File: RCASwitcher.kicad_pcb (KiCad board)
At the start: 2 copper layers, 128.5 x 75.5 mm, 13 parts, among them J1 Connector_RCA_2x3_REB, J2 Connector_RCA_2x3_REB, J3 Connector_RCA_2x3_REB, J4 Connector_RCA_2x3_REB, J5 Connector_RCA_2x3_REB, J6 Connector_RCA_2x3_REB, SW1 SW_SPDT_3x2_REB, SW2 SW_SPDT_3x2_REB, SW3 SW_SPDT_3x2_REB, SW4 SW_SPDT_3x2_REB, SW5 SW_SPDT_3x2_REB

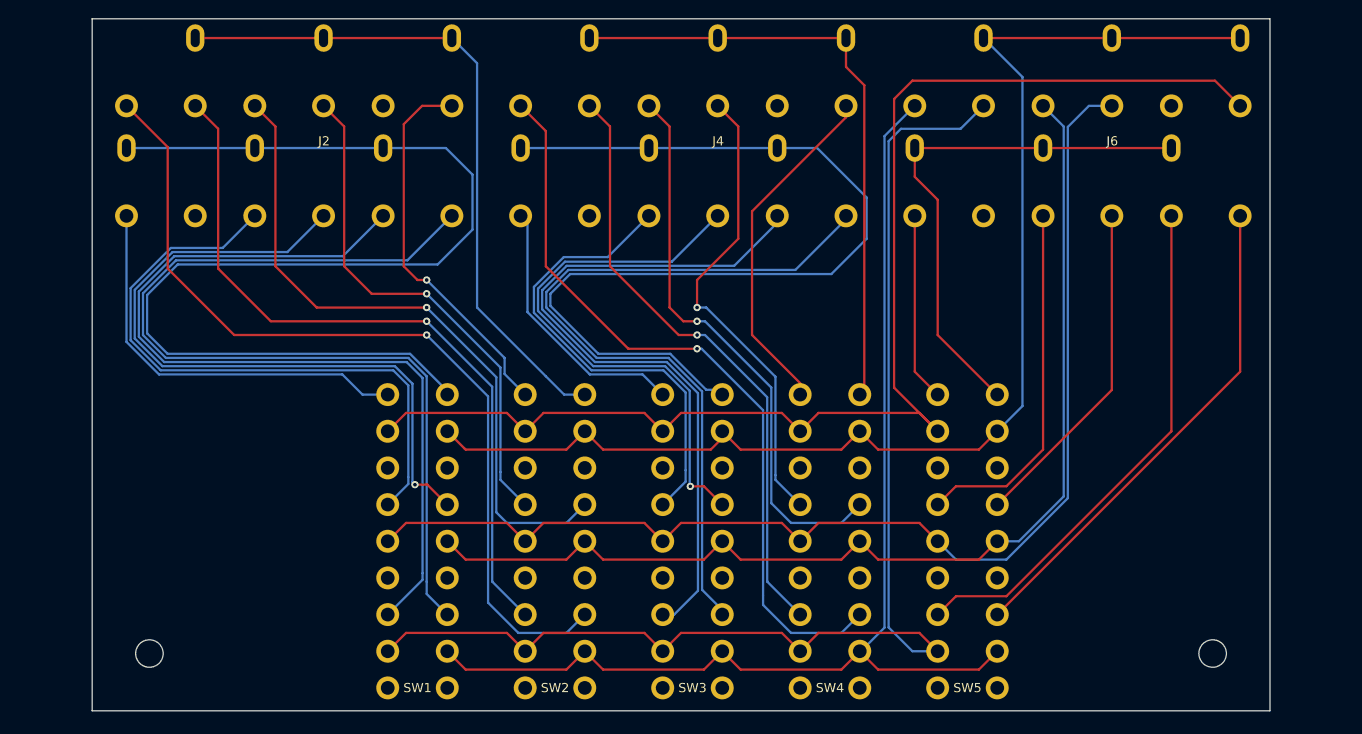
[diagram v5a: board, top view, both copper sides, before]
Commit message: Expand board a little to add mount points
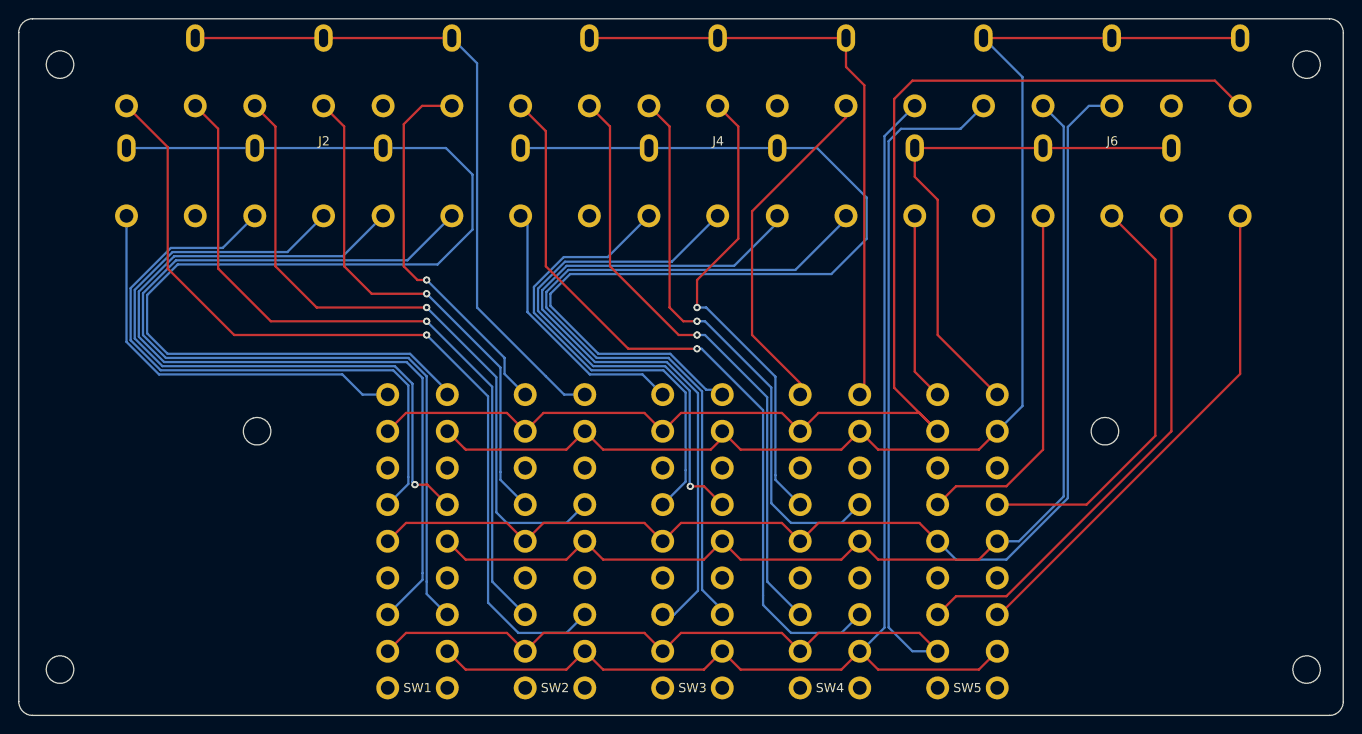
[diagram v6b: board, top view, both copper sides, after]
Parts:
- added REF**: MountingHole_3mm, MountingHole:MountingHole_3mm, F.Cu at (28.0, 70.0)
- added REF**: MountingHole_3mm, MountingHole:MountingHole_3mm, F.Cu at (142.0, 110.0)
- added REF**: MountingHole_3mm, MountingHole:MountingHole_3mm, F.Cu at (49.5, 110.0)
- added REF**: MountingHole_3mm, MountingHole:MountingHole_3mm, F.Cu at (164.0, 70.0)
- moved REF** 10.4 mm to (164.0, 136.0)
- moved REF** 9.91 mm to (28.0, 136.0)
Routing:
- net /R_5: track 36.7 -> 46.3 mm
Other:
- board size 128.5 x 75.5 mm -> 144.5 x 76 mm
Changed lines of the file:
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@@
       (net 28 "/GND_4") (pinfunction "GND") (pintype "passive"))
+  )
+  (footprint "MountingHole:MountingHole_3mm" (layer "F.Cu")
+    (at 28 70)
+    (descr "Mounting Hole 3mm, no annular")
+    (tags "mounting hole 3mm no annular")
+    (attr exclude_from_pos_files exclude_from_bom)
+    (fp_text reference "REF**" (at 0 -4) (layer "F.SilkS") hide
+      (effects (font (size 1 1) (thickness 0.15)))
+    )
+    (fp_text value "MountingHole_3mm" (at 0 4) (layer "F.Fab")
+      (effects (font (size 1 1) (thickness 0.15)))
+    )
+    (fp_text user "${REFERENCE}" (at 0 0) (layer "F.Fab")
+      (effects (font (size 1 1) (thickness 0.15)))
+    )
+    (fp_circle (center 0 0) (end 3 0) (layer "Cmts.User") (width 0.15) (fill none))
+    (fp_circle (center 0 0) (end 3.25 0) (layer "F.CrtYd") (width 0.05) (fill none))
+    (pad "" np_thru_hole circle (at 0 0) (size 3 3) (drill 3) (layers *.Cu *.Mask))
   )
   (footprint "User:SW_SPDT_3x2_REB" (layer "F.Cu")
@@
       (net 35 "/GND_5") (pinfunction "C") (pintype "passive"))
   )
+  (footprint "MountingHole:MountingHole_3mm" (layer "F.Cu")
+    (at 142 110)
+    (descr "Mounting Hole 3mm, no annular")
+    (tags "mounting hole 3mm no annular")
+    (attr exclude_from_pos_files exclude_from_bom)
+    (fp_text reference "REF**" (at 0 -4) (layer "F.SilkS") hide
+      (effects (font (size 1 1) (thickness 0.15)))
+    )
+    (fp_text value "MountingHole_3mm" (at 0 4) (layer "F.Fab")
+      (effects (font (size 1 1) (thickness 0.15)))
+    )
+    (fp_text user "${REFERENCE}" (at 0 0) (layer "F.Fab")
+      (effects (font (size 1 1) (thickness 0.15)))
+    )
+    (fp_circle (center 0 0) (end 3 0) (layer "Cmts.User") (width 0.15) (fill none))
+    (fp_circle (center 0 0) (end 3.25 0) (layer "F.CrtYd") (width 0.05) (fill none))
+    (pad "" np_thru_hole circle (at 0 0) (size 3 3) (drill 3) (layers *.Cu *.Mask))
+  )
   (footprint "User:Connector_RCA_2x3_REB" (layer "F.Cu")
     (at 142.75 74.5)
@@
     (pad "9" thru_hole oval (at -14 -7.4) (size 2 3) (drill oval 1 2) (layers *.Cu *.Mask)
       (net 42 "/GND_out") (pinfunction "GND") (pintype "passive"))
+  )
+  (footprint "MountingHole:MountingHole_3mm" (layer "F.Cu")
+    (at 49.5 110)
+    (descr "Mounting Hole 3mm, no annular")
+    (tags "mounting hole 3mm no annular")
+    (attr exclude_from_pos_files exclude_from_bom)
+    (fp_text reference "REF**" (at 0 -4) (layer "F.SilkS") hide
+      (effects (font (size 1 1) (thickness 0.15)))
+    )
+    (fp_text value "MountingHole_3mm" (at 0 4) (layer "F.Fab")
+      (effects (font (size 1 1) (thickness 0.15)))
+    )
+    (fp_text user "${REFERENCE}" (at 0 0) (layer "F.Fab")
+      (effects (font (size 1 1) (thickness 0.15)))
+    )
+    (fp_circle (center 0 0) (end 3 0) (layer "Cmts.User") (width 0.15) (fill none))
+    (fp_circle (center 0 0) (end 3.25 0) (layer "F.CrtYd") (width 0.05) (fill none))
+    (pad "" np_thru_hole circle (at 0 0) (size 3 3) (drill 3) (layers *.Cu *.Mask))
   )
   (footprint "User:SW_SPDT_3x2_REB" locked (layer "F.Cu")
@@
   )
   (footprint "MountingHole:MountingHole_3mm" (layer "F.Cu")
-    (at 37.75 134.25)
+    (at 28 136)
     (descr "Mounting Hole 3mm, no annular")
     (tags "mounting hole 3mm no annular")
@@
   )
   (footprint "MountingHole:MountingHole_3mm" (layer "F.Cu")
-    (at 153.75 134.25)
+    (at 164 136)
+    (descr "Mounting Hole 3mm, no annular")
+    (tags "mounting hole 3mm no annular")
+    (attr exclude_from_pos_files exclude_from_bom)
+    (fp_text reference "REF**" (at 0 -4) (layer "F.SilkS") hide
+      (effects (font (size 1 1) (thickness 0.15)))
+    )
+    (fp_text value "MountingHole_3mm" (at 0 4) (layer "F.Fab")
+      (effects (font (size 1 1) (thickness 0.15)))
+    )
+    (fp_text user "${REFERENCE}" (at 0 0) (layer "F.Fab")
+      (effects (font (size 1 1) (thickness 0.15)))
+    )
+    (fp_circle (center 0 0) (end 3 0) (layer "Cmts.User") (width 0.15) (fill none))
+    (fp_circle (center 0 0) (end 3.25 0) (layer "F.CrtYd") (width 0.05) (fill none))
+    (pad "" np_thru_hole circle (at 0 0) (size 3 3) (drill 3) (layers *.Cu *.Mask))
+  )
+  (footprint "MountingHole:MountingHole_3mm" (layer "F.Cu")
+    (at 164 70)
     (descr "Mounting Hole 3mm, no annular")
     (tags "mounting hole 3mm no annular")
@@
       (net 7 "/GND_1") (pinfunction "GND") (pintype "passive"))
   )
-  (gr_rect (start 31.5 65) (end 160 140.5) (layer "Edge.Cuts") (width 0.1) (fill none))
+  (gr_arc (start 23.5 66.5) (mid 23.93934 65.43934) (end 25 65) (layer "Edge.Cuts") (width 0.1))
+  (gr_line (start 25 141) (end 166.5 141) (layer "Edge.Cuts") (width 0.1))
+  (gr_line (start 166.5 65) (end 25 65) (layer "Edge.Cuts") (width 0.1))
+  (gr_arc (start 168 139.5) (mid 167.56066 140.56066) (end 166.5 141) (layer "Edge.Cuts") (width 0.1))
+  (gr_line (start 23.5 66.5) (end 23.5 139.5) (layer "Edge.Cuts") (width 0.1))
+  (gr_arc (start 25 141) (mid 23.93934 140.56066) (end 23.5 139.5) (layer "Edge.Cuts") (width 0.1))
+  (gr_line (start 168 139.5) (end 168 66.5) (layer "Edge.Cuts") (width 0.1))
+  (gr_arc (start 166.5 65) (mid 167.56066 65.43934) (end 168 66.5) (layer "Edge.Cuts") (width 0.1))
   (gr_text "Print out and test spacing on paper!" (at 36.5 58) (layer "User.1")
     (effects (font (size 1 1) (thickness 0.15)) (justify left))
@@
   (segment (start 121.25 103.5) (end 123.75 106) (width 0.25) (layer "F.Cu") (net 31))
   (segment (start 121.25 86.5) (end 121.25 103.5) (width 0.25) (layer "F.Cu") (net 31))
-  (segment (start 156.75 86.5) (end 156.75 103.5) (width 0.25) (layer "F.Cu") (net 32))
-  (segment (start 156.75 103.5) (end 130.25 130) (width 0.25) (layer "F.Cu") (net 32))
-  (segment (start 142.75 86.5) (end 142.75 105.5) (width 0.25) (layer "F.Cu") (net 33))
-  (segment (start 142.75 105.5) (end 130.25 118) (width 0.25) (layer "F.Cu") (net 33))
+  (segment (start 156.75 103.75) (end 130.5 130) (width 0.25) (layer "F.Cu") (net 32))
+  (segment (start 156.75 86.5) (end 156.75 103.75) (width 0.25) (layer "F.Cu") (net 32))
+  (segment (start 130.5 130) (end 130.25 130) (width 0.25) (layer "F.Cu") (net 32))
+  (segment (start 147.5 91.25) (end 147.5 110.5) (width 0.25) (layer "F.Cu") (net 33))
+  (segment (start 140 118) (end 130.25 118) (width 0.25) (layer "F.Cu") (net 33))
+  (segment (start 142.75 86.5) (end 147.5 91.25) (width 0.25) (layer "F.Cu") (net 33))
+  (segment (start 147.5 110.5) (end 140 118) (width 0.25) (layer "F.Cu") (net 33))
   (segment (start 123.75 84.738551) (end 123.75 99.5) (width 0.25) (layer "F.Cu") (net 35))
   (segment (start 121.25 82.238551) (end 123.75 84.738551) (width 0.25) (layer "F.Cu") (net 35))

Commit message: Adds 3d model and gerbers for fabrication
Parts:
- moved REF** 0.50 mm to (163.5, 136.0)
- moved REF** 0.50 mm to (163.5, 70.0)
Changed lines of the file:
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@@
   )
   (footprint "MountingHole:MountingHole_3mm" (layer "F.Cu")
-    (at 164 136)
+    (at 163.5 136)
     (descr "Mounting Hole 3mm, no annular")
     (tags "mounting hole 3mm no annular")
@@
   )
   (footprint "MountingHole:MountingHole_3mm" (layer "F.Cu")
-    (at 164 70)
+    (at 163.5 70)
     (descr "Mounting Hole 3mm, no annular")
     (tags "mounting hole 3mm no annular")

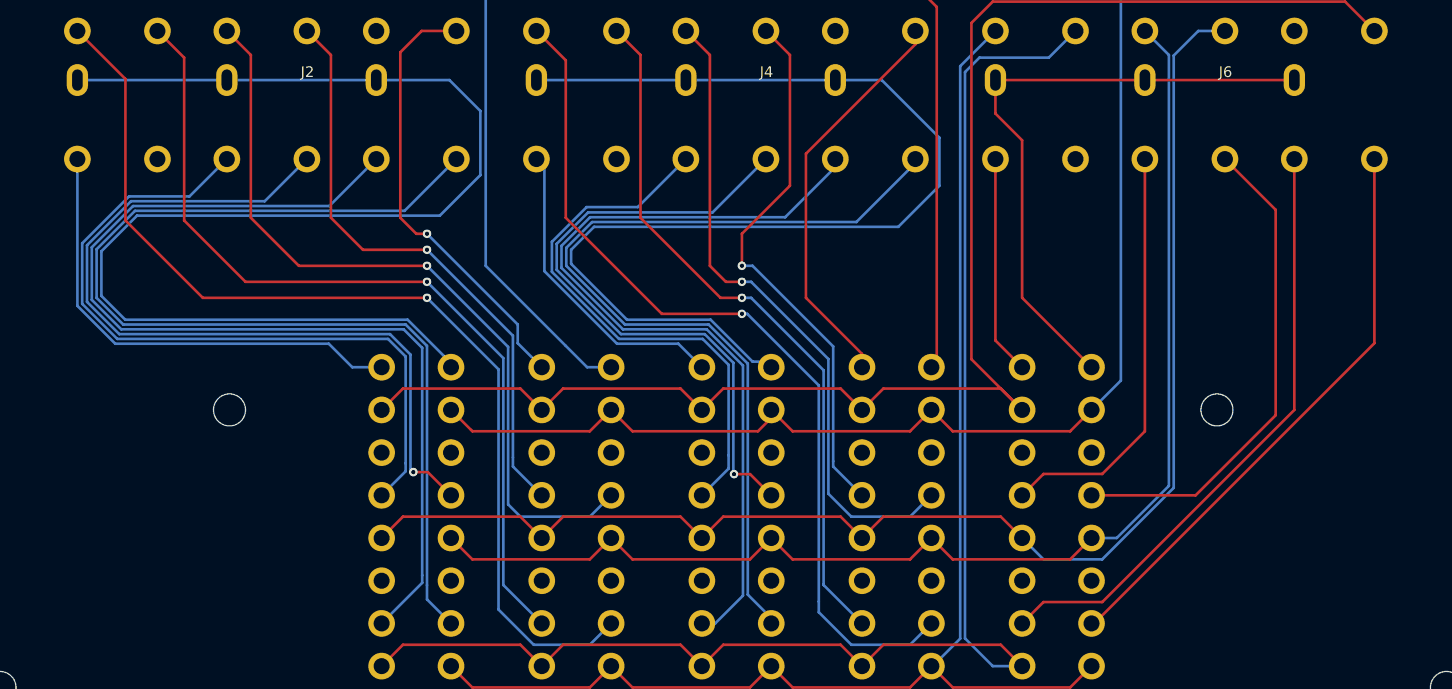
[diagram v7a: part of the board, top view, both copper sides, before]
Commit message: Nudge rows apart a little to fix overlap
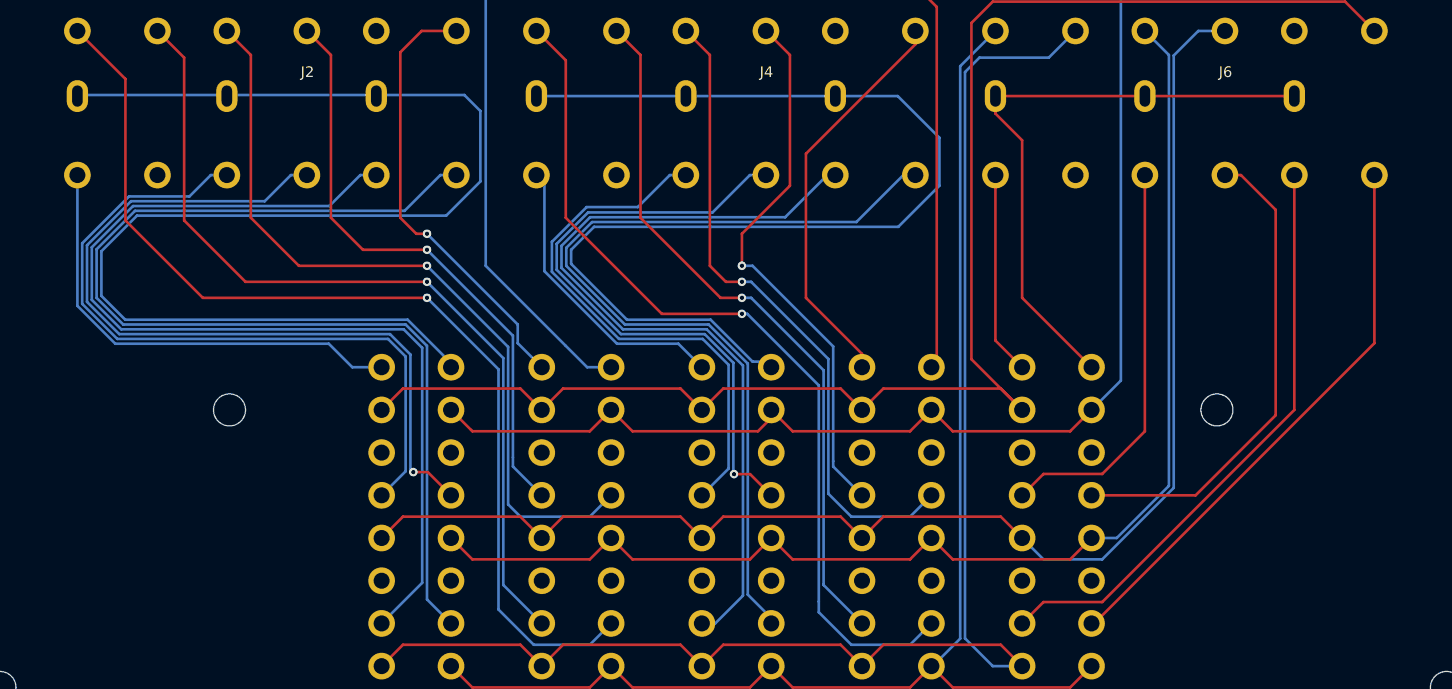
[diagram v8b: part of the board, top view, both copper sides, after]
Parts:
- moved J1 1.50 mm to (49.2, 88.0)
- moved J3 1.50 mm to (92.2, 88.0)
- moved J5 1.50 mm to (135.2, 88.0)
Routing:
- net /Pr_3: track 29.3 -> 27.8 mm
- net /Y_5: track 57.3 -> 55.8 mm
- net /Pr_5: track 20.5 -> 19.0 mm
- net /Pr_1: track 44.6 -> 43.1 mm
- net /Pb_5: track 39.5 -> 38.0 mm
- net /L_5: track 54.6 -> 53.1 mm
- net /GND_5: track 58.6 -> 57.1 mm
- net /Y_3: track 78.8 -> 77.7 mm
- net /L_3: track 84.1 -> 83.3 mm
- net /GND_3: track 105.6 -> 104.9 mm
- net /R_5: track 46.3 -> 45.7 mm
- net /R_3: track 60.2 -> 59.6 mm
- net /Pb_3: track 52.0 -> 51.4 mm
- net /Y_1: track 95.2 -> 94.6 mm
- net /R_1: track 77.1 -> 76.5 mm
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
